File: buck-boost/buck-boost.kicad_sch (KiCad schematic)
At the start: 29 parts, among them U16 LMR33630ADDA, U18 LMR62014XMF_NOPB

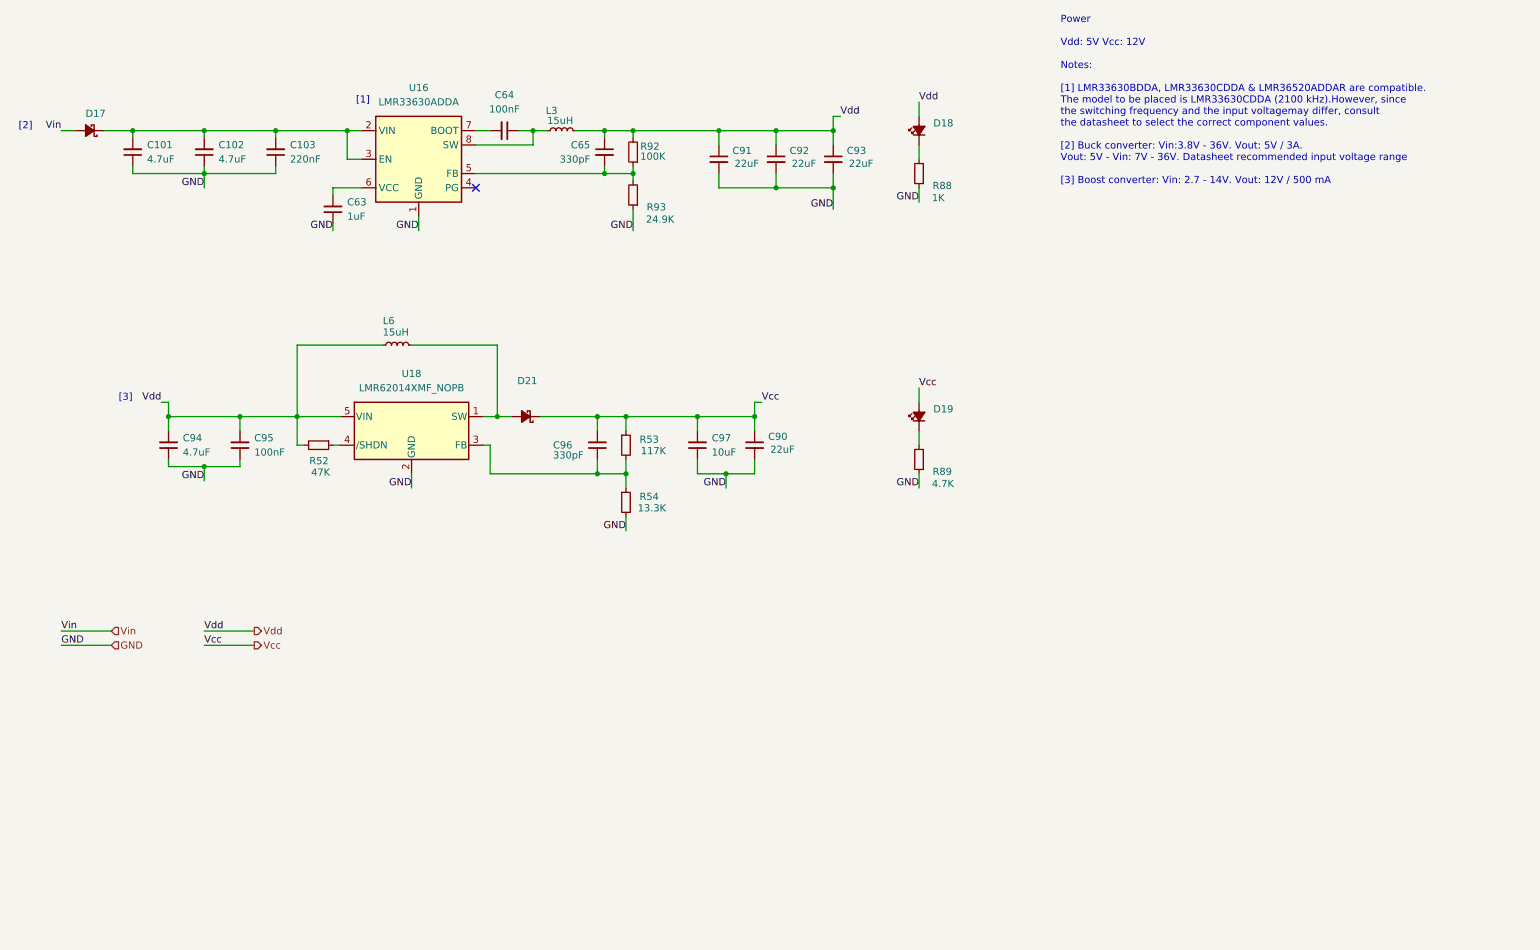
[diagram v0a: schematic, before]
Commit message: Some errors in the schematics were corrected. PCB file V1.0
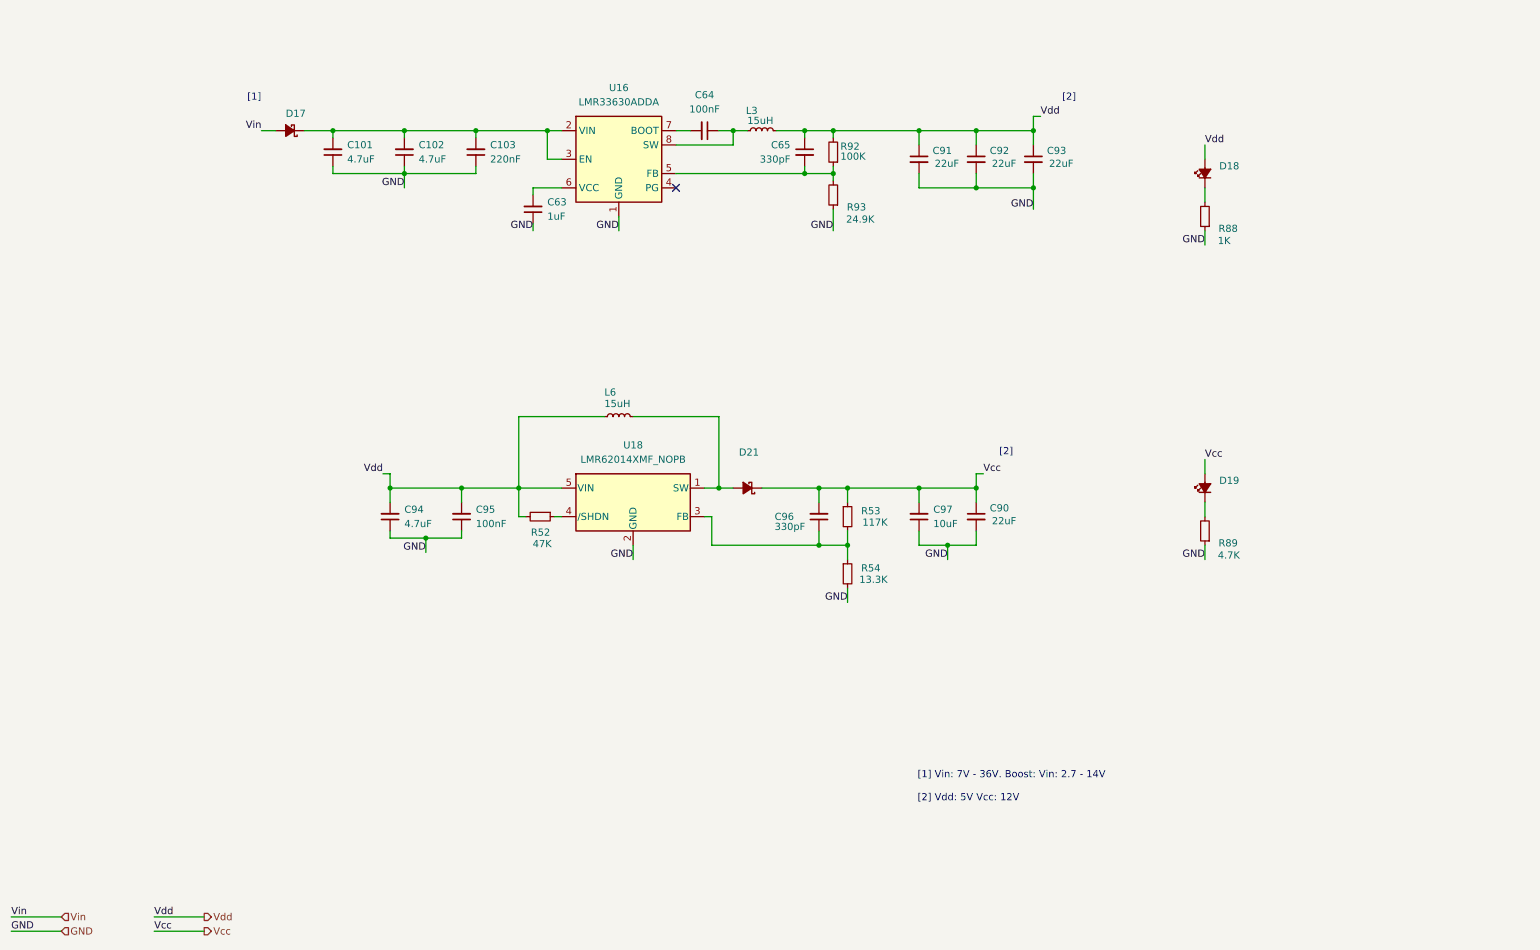
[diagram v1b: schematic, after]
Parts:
- C101, C102, C97: footprint Capacitor_SMD:C_1210_3225Metric_Pad1.33x2.70mm_HandSolder -> Capacitor_SMD:C_0805_2012Metric_Pad1.18x1.45mm_HandSolder
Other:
- note added: "[1] Vin: 7V - 36V. Boost: Vin: 2.7 - 14V [2] Vdd: 5V Vcc: 12V"
- note removed: "Power Vdd: 5V Vcc: 12V Notes: [1] LMR33630BDDA, LMR33630CDDA & LMR36520ADDAR are compatible. The model to be placed is LMR33630CDDA (2100 kHz).However, since the switching frequency and the input voltagemay differ, consult the datasheet to select the correct component values. [2] Buck converter: Vin:3.8V - 36V. Vout: 5V / 3A. Vout: 5V - Vin: 7V - 36V. Datasheet recommended input voltage range [3]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"
- note removed: "[3]"
- moved on the sheet: C101, C102, C103, C63, C64, C65, C90, C91, C92, C93, C94, C95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
